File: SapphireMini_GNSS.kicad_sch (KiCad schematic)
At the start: 13 parts, among them J401 DNP Conn_01x01_Male, J402 Conn_01x04_Male, J403 ExtPPS, U402 SAM-M8Q-0-10

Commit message: End of Day
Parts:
- D402: symbol sapphireMini:LED_G -> Device:LED
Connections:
- net TIMEPULSE: now also D402.2 (A); no longer D402.1 (A)
- net at R403.2, R404.2: now also D402.1 (K); no longer D402.2 (K)
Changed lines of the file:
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@@
     (pin "9")
   )
-  (symbol (lib_id "sapphireMini:LED_G") (at 111.76 107.95 90) (unit 1)
+  (symbol (lib_name "LED_1") (lib_id "Device:LED") (at 111.76 107.95 90) (unit 1)
     (in_bom yes) (on_board yes)
     (property "Reference" "D402" (id 0) (at 113.1004 101.2372 0)

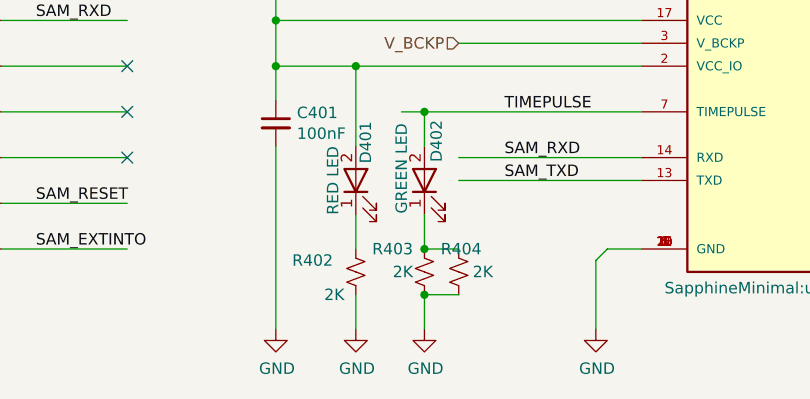
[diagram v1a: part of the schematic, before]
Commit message: Updated to correct wiring of IIM42351
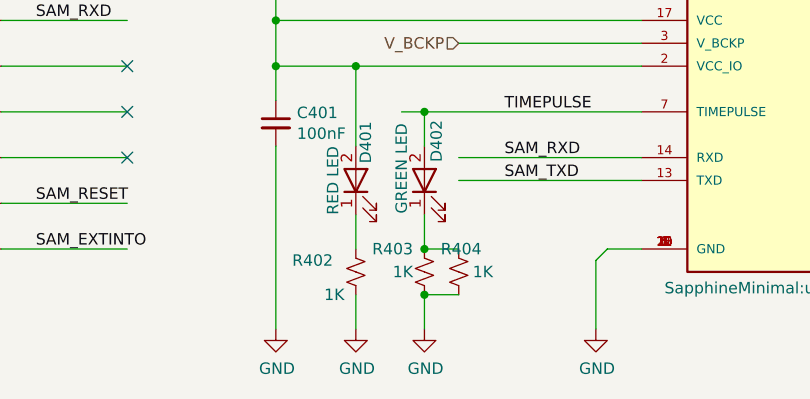
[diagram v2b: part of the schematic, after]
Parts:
- R402, R403, R404: value 2K -> 1K; MPN CRCW06032K00FKEAC -> CRCW06031K00FKEAC
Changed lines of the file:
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@@
       (effects (font (size 1.27 1.27)) (justify left))
     )
-    (property "Value" "2K" (id 1) (at 110.49 118.11 0)
+    (property "Value" "1K" (id 1) (at 110.49 118.11 0)
       (effects (font (size 1.27 1.27)) (justify left))
     )
@@
       (effects (font (size 1.27 1.27)) hide)
     )
-    (property "MPN" "CRCW06032K00FKEAC" (id 6) (at 111.76 118.11 0)
+    (property "MPN" "CRCW06031K00FKEAC" (id 6) (at 111.76 118.11 0)
       (effects (font (size 1.27 1.27)) hide)
     )
@@
       (effects (font (size 1.27 1.27)) hide)
     )
-    (property "Description" "2 kOhms ±1% 0.1W, 1/10W Chip Resistor 0603" (id 13) (at 111.76 118.11 0)
+    (property "Description" "1 kOhms ±1% 0.1W, 1/10W Chip Resistor 0603" (id 13) (at 111.76 118.11 0)
       (effects (font (size 1.27 1.27)) hide)
     )
@@
       (effects (font (size 1.27 1.27)) (justify left))
     )
-    (property "Value" "2K" (id 1) (at 102.87 120.65 0)
+    (property "Value" "1K" (id 1) (at 102.87 120.65 0)
       (effects (font (size 1.27 1.27)) (justify left))
     )
@@
       (effects (font (size 1.27 1.27)) hide)
     )
-    (property "MPN" "CRCW06032K00FKEAC" (id 6) (at 104.14 118.11 0)
+    (property "MPN" "CRCW06031K00FKEAC" (id 6) (at 104.14 118.11 0)
       (effects (font (size 1.27 1.27)) hide)
     )
@@
       (effects (font (size 1.27 1.27)) hide)
     )
-    (property "Description" "2 kOhms ±1% 0.1W, 1/10W Chip Resistor 0603" (id 13) (at 104.14 118.11 0)
+    (property "Description" "1 kOhms ±1% 0.1W, 1/10W Chip Resistor 0603" (id 13) (at 104.14 118.11 0)
       (effects (font (size 1.27 1.27)) hide)
     )
@@
       (effects (font (size 1.27 1.27)) (justify left))
     )
-    (property "Value" "2K" (id 1) (at 119.38 118.11 0)
+    (property "Value" "1K" (id 1) (at 119.38 118.11 0)
       (effects (font (size 1.27 1.27)) (justify left))
     )
@@
       (effects (font (size 1.27 1.27)) hide)
     )
-    (property "MPN" "CRCW06032K00FKEAC" (id 6) (at 115.57 118.11 0)
+    (property "MPN" "CRCW06031K00FKEAC" (id 6) (at 115.57 118.11 0)
       (effects (font (size 1.27 1.27)) hide)
     )
@@
       (effects (font (size 1.27 1.27)) hide)
     )
-    (property "Description" "2 kOhms ±1% 0.1W, 1/10W Chip Resistor 0603" (id 13) (at 115.57 118.11 0)
-      (effects (font (size 1.27 1.27)) hide)
-    )
+    (property "Description" "1 kOhms ±1% 0.1W, 1/10W Chip Resistor 0603" (id 13) (at 115.57 118.11 0)
+      (effects (font (size 1.27 1.27)) hide)
+    )
